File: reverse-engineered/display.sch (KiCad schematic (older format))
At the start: 36 parts, among them T1 PHOTO-TRANSISTOR, T2 PHOTO-TRANSISTOR, T4 PHOTO-TRANSISTOR

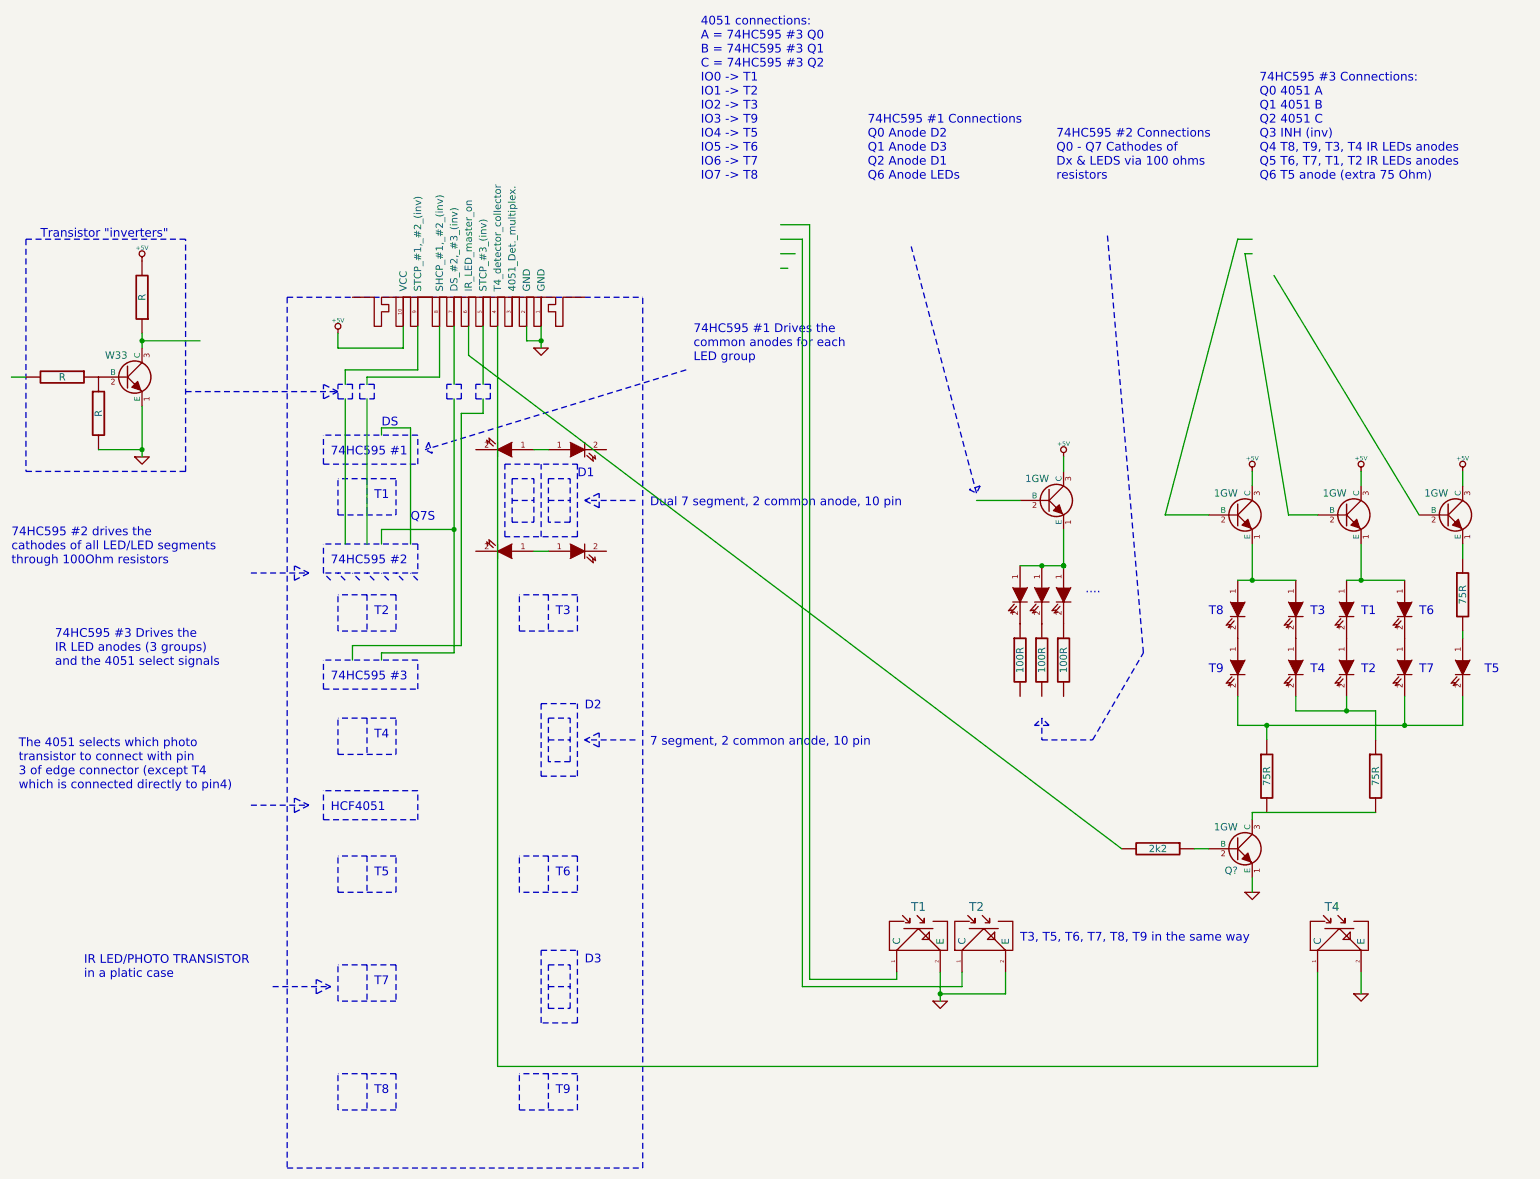
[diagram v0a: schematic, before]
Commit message: Some more reverse engineering
Started measure with oscilloscope, seems
to get funny measurements. Will have to do
them again.
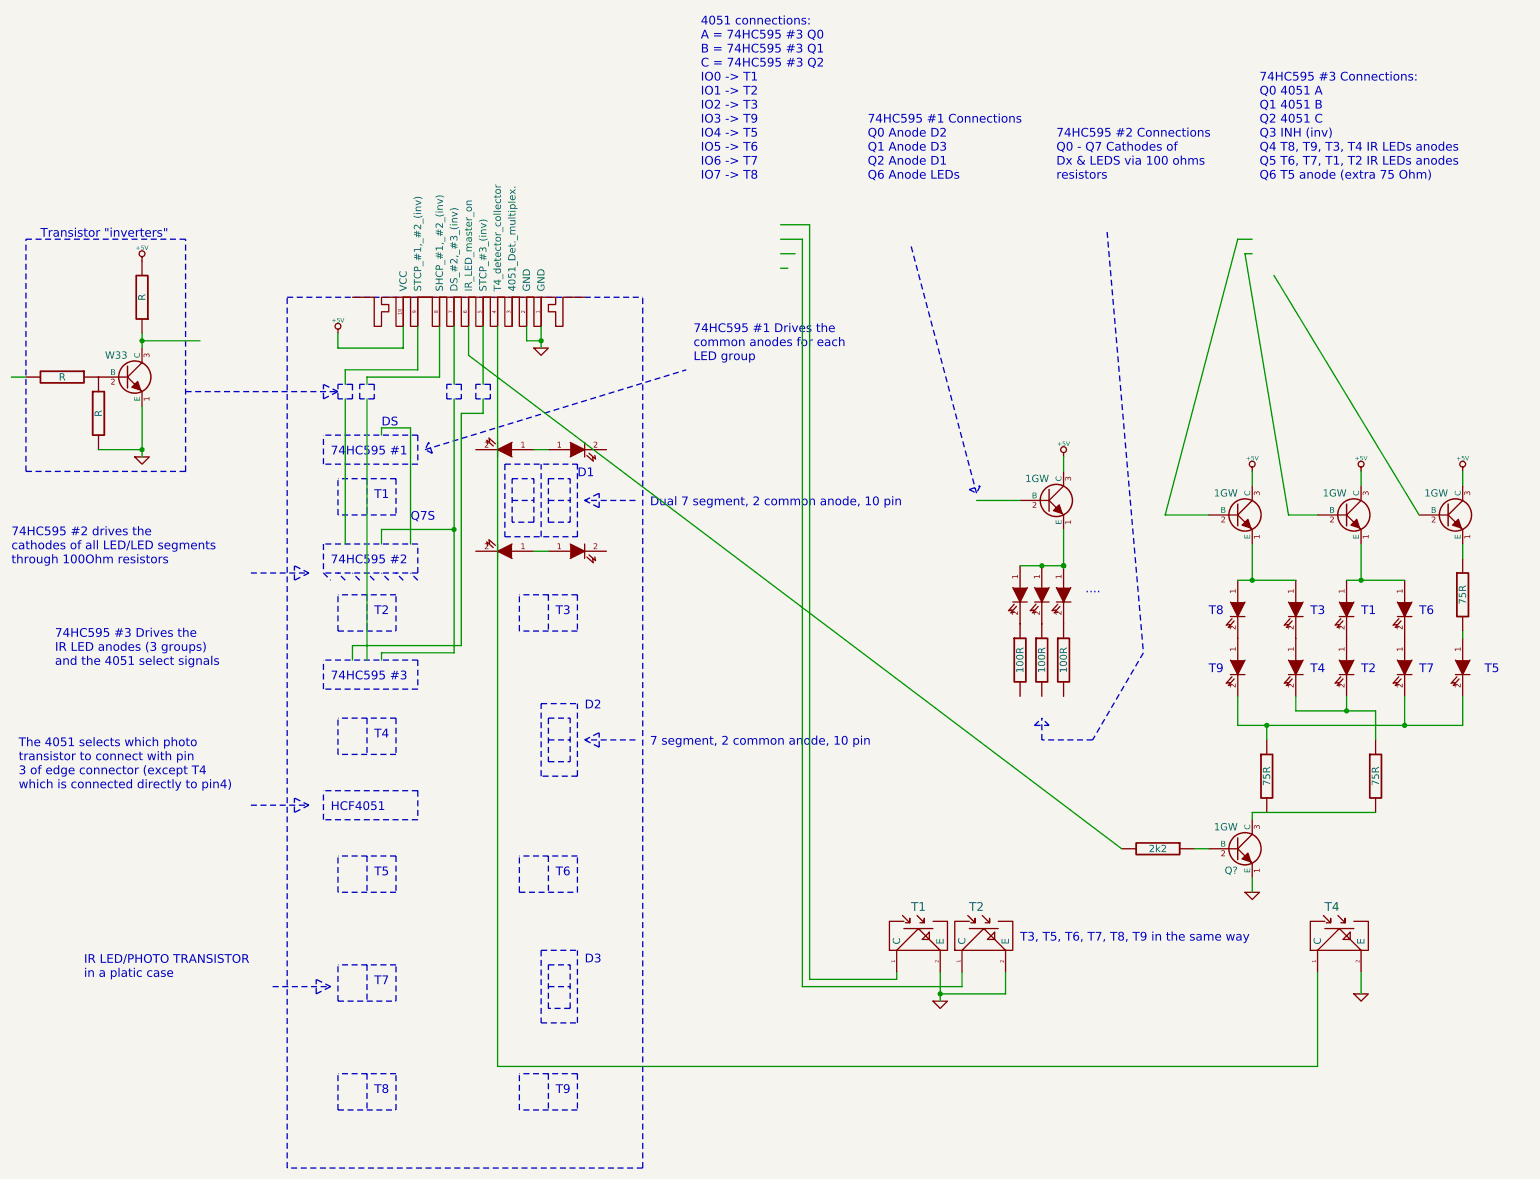
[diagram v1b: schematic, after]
